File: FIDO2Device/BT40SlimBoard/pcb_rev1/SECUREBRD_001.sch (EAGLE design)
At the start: 32 parts, among them CN1 2137160001, CN2 IF_4PIN, CN4 IF_3PIN_SOL, SW3 SKTADAE010, SW4 SKRPACE010, SW5 SKRPACE010, U1 BT40, U2 XC6206P332MR-G

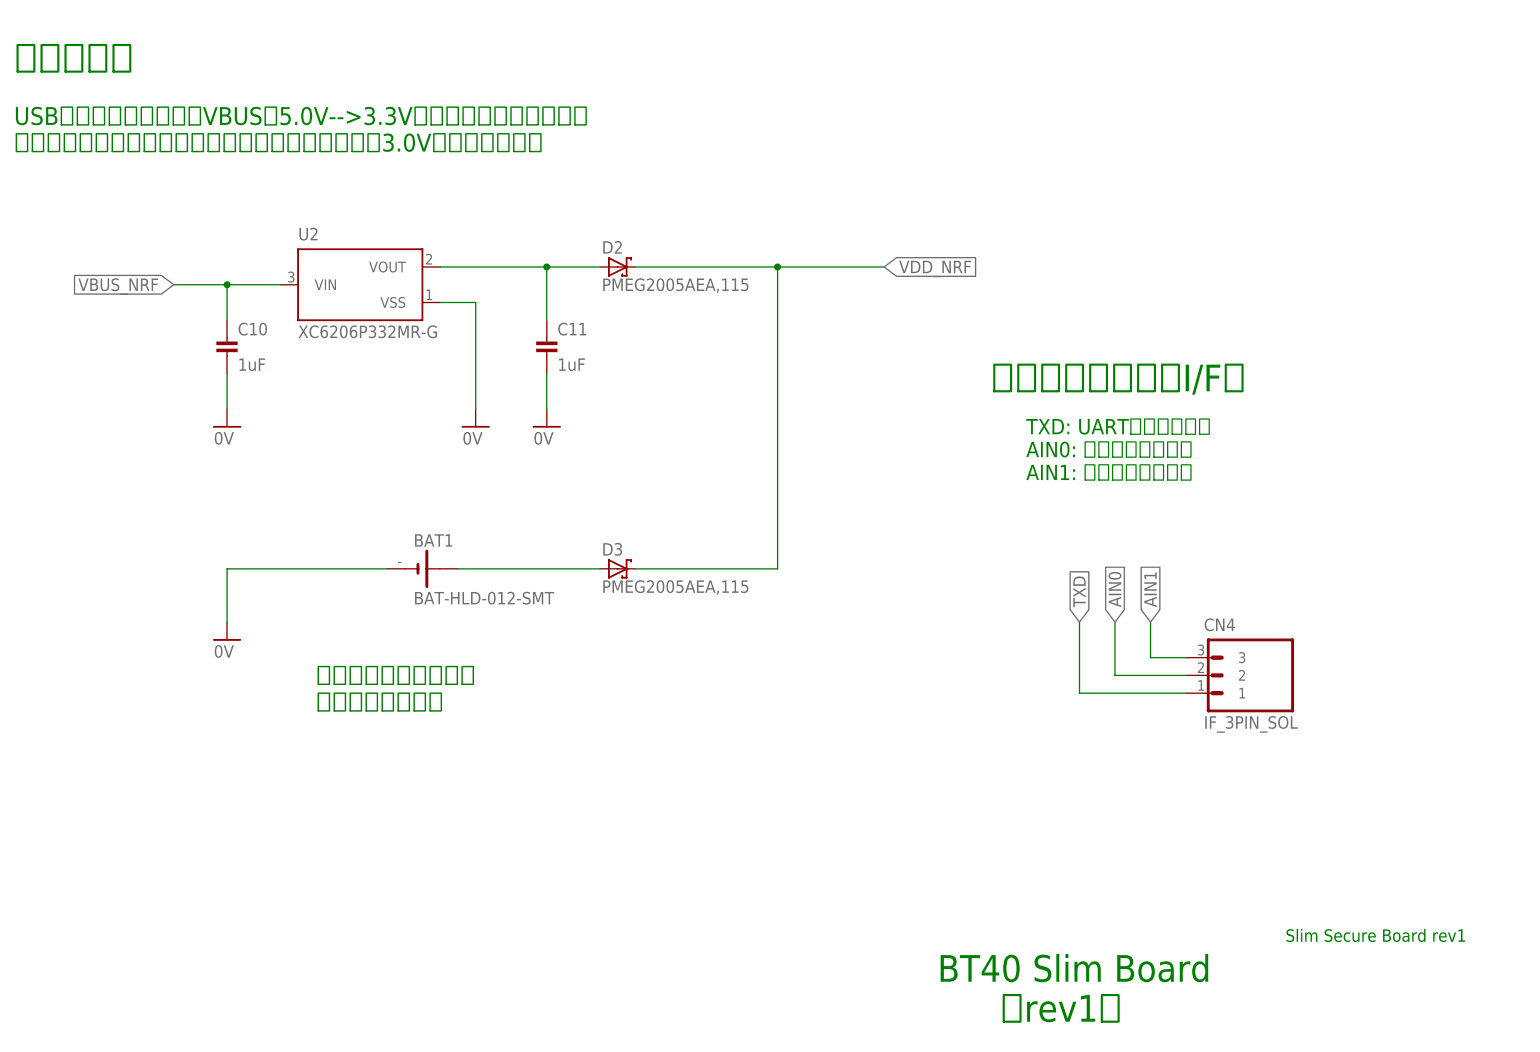
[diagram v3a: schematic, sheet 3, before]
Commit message: 回路図を更新
・降圧器を「ADP122ACPZ-3.3-R7」に差し替え
（小型化＆部品入手性を考慮した措置）
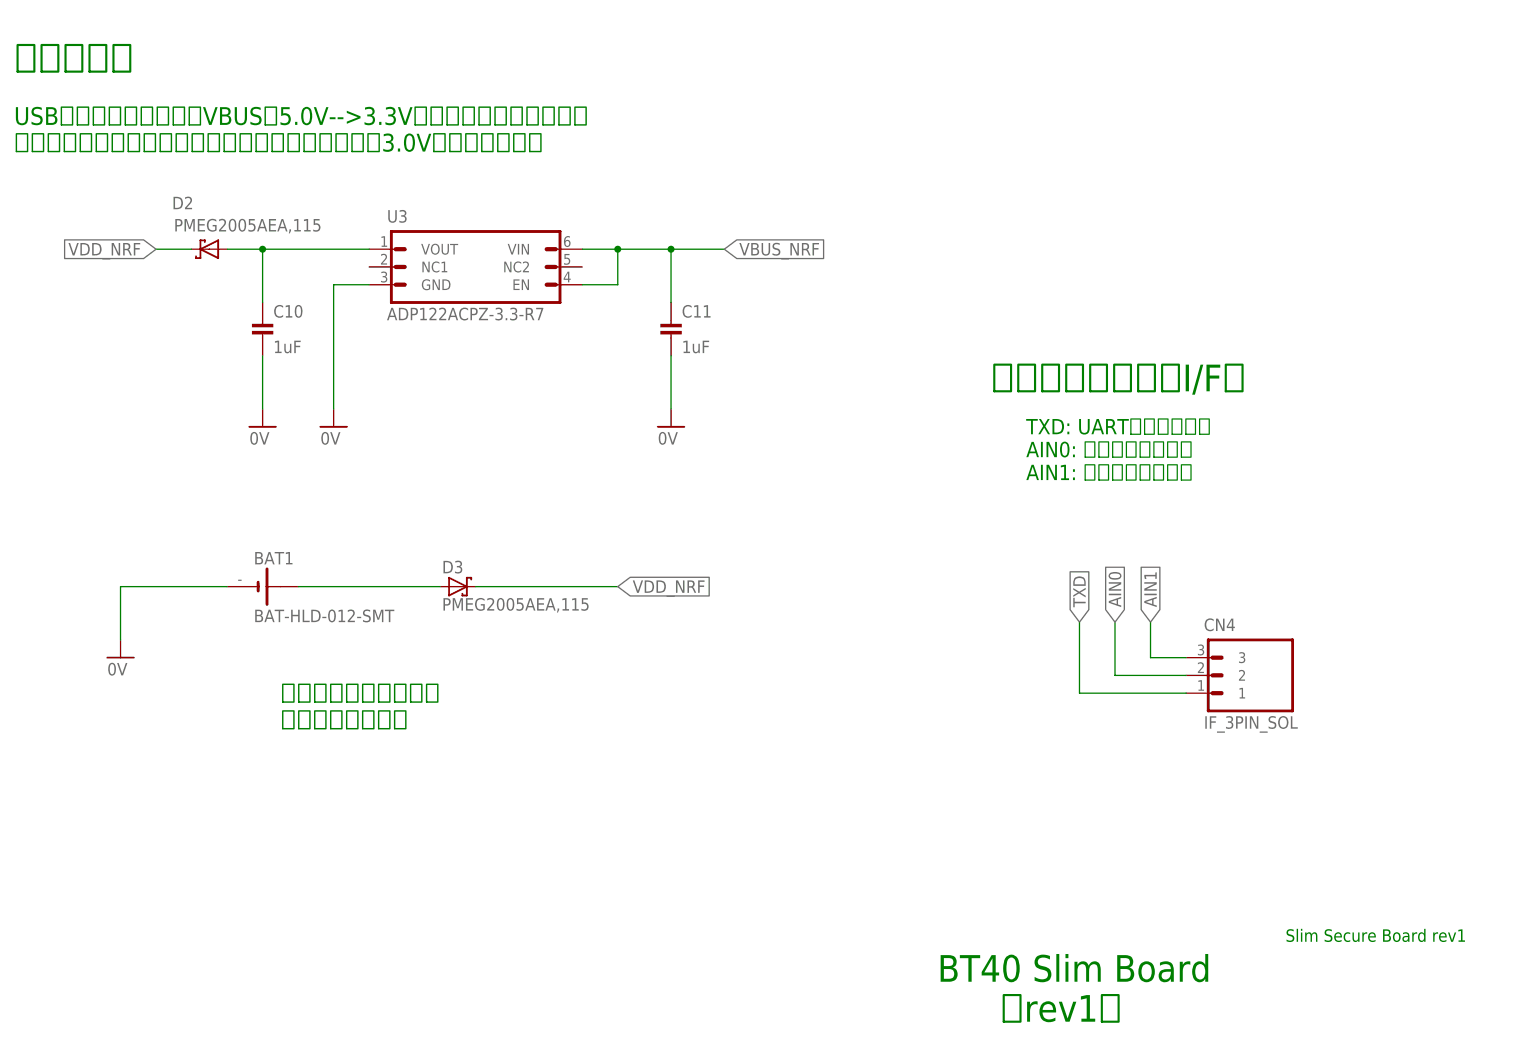
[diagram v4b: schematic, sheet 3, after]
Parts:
- removed U2: XC6206P332MR-G, Parts:XC6206P332MR-G
- added U3: ADP122ACPZ-3.3-R7, ICs:ADP122ACPZ-3.3-R7
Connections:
- removed net N$4: C11.1, D2.A, U2.VOUT
- new net N$3: C10.1, D2.A, U3.VOUT
- net 0V: now also U3.GND; no longer U2.VSS
- net VBUS_NRF: now also C11.1, U3.EN, U3.VIN; no longer C10.1, U2.VIN
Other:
- moved on the sheet: BAT1, C10, C11, D2, D3
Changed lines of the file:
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@@
 <setting verticaltext="up"/>
 </settings>
-<grid distance="0.1" unitdist="inch" unit="inch" style="lines" multiple="1" display="no" altdistance="0.01" altunitdist="inch" altunit="inch"/>
+<grid distance="0.1" unitdist="inch" unit="inch" style="lines" multiple="1" display="yes" altdistance="0.01" altunitdist="inch" altunit="inch"/>
 <layers>
 <layer number="1" name="Top" color="4" fill="1" visible="no" active="no"/>
@@
 <part name="LD2" library="Parts" deviceset="APHD1608" device="LSURCK"/>
 <part name="LD4" library="Parts" deviceset="APTD1608" device="LVBC/D"/>
-<part name="U2" library="Parts" deviceset="XC6206" device="P332MR-G"/>
 <part name="C10" library="Parts" deviceset="CAP" device="_0603" value="1uF"/>
 <part name="C11" library="Parts" deviceset="CAP" device="_0603" value="1uF"/>
@@
 <part name="CN1" library="Connectors" deviceset="2137160001" device=""/>
 <part name="R2" library="Parts" deviceset="RESISTOR" device="_0402" value="5.1k"/>
+<part name="U3" library="ICs" deviceset="ADP122" device="ACPZ-3.3-R7"/>
 </parts>
 <sheets>
@@
 <text x="35.56" y="139.7" size="2.54" layer="91" align="top-left">USBポートに装着時は、VBUSの5.0V--&gt;3.3Vに降圧して供給します。
 乾電池ホルダーにボタン乾電池を装着した場合は、3.0Vを供給します。</text>
-<text x="78.74" y="53.34" size="2.54" layer="91">ボタン乾電池ケースは
+<text x="73.66" y="50.8" size="2.54" layer="91">ボタン乾電池ケースは
 基板の表面に実装</text>
 <text x="175.26" y="99.06" size="3.81" layer="91">ユーティリティーI/F部</text>
@@
 <instances>
 <instance part="FRAME3" gate="G$1" x="0" y="0"/>
-<instance part="U2" gate="G$1" x="73.66" y="116.84"/>
-<instance part="C10" gate="G$1" x="66.04" y="109.22"/>
-<instance part="C11" gate="G$1" x="111.76" y="109.22"/>
-<instance part="GND16" gate="1" x="101.6" y="93.98"/>
-<instance part="GND17" gate="1" x="66.04" y="93.98"/>
-<instance part="GND18" gate="1" x="111.76" y="93.98"/>
-<instance part="D2" gate="G$1" x="121.92" y="116.84"/>
-<instance part="D3" gate="G$1" x="121.92" y="73.66"/>
-<instance part="BAT1" gate="G$1" x="93.98" y="73.66"/>
-<instance part="GND19" gate="1" x="66.04" y="63.5"/>
+<instance part="C10" gate="G$1" x="71.12" y="111.76"/>
+<instance part="C11" gate="G$1" x="129.54" y="111.76"/>
+<instance part="GND16" gate="1" x="71.12" y="93.98"/>
+<instance part="GND17" gate="1" x="81.28" y="93.98"/>
+<instance part="GND18" gate="1" x="129.54" y="93.98"/>
+<instance part="D2" gate="G$1" x="63.5" y="119.38" smashed="yes" rot="R180">
+<attribute name="NAME" x="58.166" y="125.095" size="1.778" layer="95"/>
+<attribute name="VALUE" x="58.42" y="121.92" size="1.778" layer="96"/>
+</instance>
+<instance part="D3" gate="G$1" x="99.06" y="71.12"/>
+<instance part="BAT1" gate="G$1" x="71.12" y="71.12"/>
+<instance part="GND19" gate="1" x="50.8" y="60.96"/>
 <instance part="CN4" gate="G$1" x="203.2" y="60.96"/>
+<instance part="U3" gate="G$1" x="86.36" y="116.84"/>
 </instances>
 <busses>
@@
 <net name="0V" class="0">
 <segment>
-<pinref part="C10" gate="G$1" pin="2"/>
-<pinref part="GND17" gate="1" pin="0V"/>
-<wire x1="66.04" y1="101.6" x2="66.04" y2="96.52" width="0.1524" layer="91"/>
-</segment>
-<segment>
-<pinref part="U2" gate="G$1" pin="VSS"/>
-<pinref part="GND16" gate="1" pin="0V"/>
-<wire x1="96.52" y1="111.76" x2="101.6" y2="111.76" width="0.1524" layer="91"/>
-<wire x1="101.6" y1="111.76" x2="101.6" y2="96.52" width="0.1524" layer="91"/>
+<pinref part="BAT1" gate="G$1" pin="-"/>
+<pinref part="GND19" gate="1" pin="0V"/>
+<wire x1="66.04" y1="71.12" x2="50.8" y2="71.12" width="0.1524" layer="91"/>
+<wire x1="50.8" y1="71.12" x2="50.8" y2="63.5" width="0.1524" layer="91"/>
 </segment>
 <segment>
 <pinref part="C11" gate="G$1" pin="2"/>
 <pinref part="GND18" gate="1" pin="0V"/>
-<wire x1="111.76" y1="101.6" x2="111.76" y2="96.52" width="0.1524" layer="91"/>
-</segment>
-<segment>
-<pinref part="BAT1" gate="G$1" pin="-"/>
-<pinref part="GND19" gate="1" pin="0V"/>
-<wire x1="88.9" y1="73.66" x2="66.04" y2="73.66" width="0.1524" layer="91"/>
-<wire x1="66.04" y1="73.66" x2="66.04" y2="66.04" width="0.1524" layer="91"/>
-</segment>
-</net>
-<net name="N$4" class="0">
-<segment>
-<pinref part="U2" gate="G$1" pin="VOUT"/>
-<wire x1="96.52" y1="116.84" x2="111.76" y2="116.84" width="0.1524" layer="91"/>
+<wire x1="129.54" y1="104.14" x2="129.54" y2="96.52" width="0.1524" layer="91"/>
+</segment>
+<segment>
+<pinref part="GND16" gate="1" pin="0V"/>
+<pinref part="C10" gate="G$1" pin="2"/>
+<wire x1="71.12" y1="96.52" x2="71.12" y2="104.14" width="0.1524" layer="91"/>
+</segment>
+<segment>
+<pinref part="GND17" gate="1" pin="0V"/>
+<wire x1="81.28" y1="96.52" x2="81.28" y2="114.3" width="0.1524" layer="91"/>
+<pinref part="U3" gate="G$1" pin="GND"/>
+<wire x1="81.28" y1="114.3" x2="86.36" y2="114.3" width="0.1524" layer="91"/>
+</segment>
+</net>
+<net name="VBUS_NRF" class="0">
+<segment>
+<wire x1="116.84" y1="119.38" x2="121.92" y2="119.38" width="0.1524" layer="91"/>
+<label x="137.16" y="119.38" size="1.778" layer="95" xref="yes"/>
+<pinref part="U3" gate="G$1" pin="VIN"/>
+<pinref part="U3" gate="G$1" pin="EN"/>
+<wire x1="121.92" y1="119.38" x2="129.54" y2="119.38" width="0.1524" layer="91"/>
+<wire x1="129.54" y1="119.38" x2="137.16" y2="119.38" width="0.1524" layer="91"/>
+<wire x1="116.84" y1="114.3" x2="121.92" y2="114.3" width="0.1524" layer="91"/>
+<wire x1="121.92" y1="114.3" x2="121.92" y2="119.38" width="0.1524" layer="91"/>
+<junction x="121.92" y="119.38"/>
 <pinref part="C11" gate="G$1" pin="1"/>
-<wire x1="111.76" y1="116.84" x2="119.38" y2="116.84" width="0.1524" layer="91"/>
-<wire x1="111.76" y1="116.84" x2="111.76" y2="109.22" width="0.1524" layer="91"/>
-<junction x="111.76" y="116.84"/>
-<pinref part="D2" gate="G$1" pin="A"/>
-</segment>
-</net>
-<net name="VBUS_NRF" class="0">
-<segment>
-<pinref part="U2" gate="G$1" pin="VIN"/>
-<pinref part="C10" gate="G$1" pin="1"/>
-<wire x1="73.66" y1="114.3" x2="66.04" y2="114.3" width="0.1524" layer="91"/>
-<wire x1="66.04" y1="114.3" x2="66.04" y2="109.22" width="0.1524" layer="91"/>
-<wire x1="66.04" y1="114.3" x2="58.42" y2="114.3" width="0.1524" layer="91"/>
-<junction x="66.04" y="114.3"/>
-<label x="58.42" y="114.3" size="1.778" layer="95" rot="R180" xref="yes"/>
+<wire x1="129.54" y1="119.38" x2="129.54" y2="111.76" width="0.1524" layer="91"/>
+<junction x="129.54" y="119.38"/>
 </segment>
 </net>
 <net name="VDD_NRF" class="0">
 <segment>
-<wire x1="124.46" y1="116.84" x2="144.78" y2="116.84" width="0.1524" layer="91"/>
-<label x="160.02" y="116.84" size="1.778" layer="95" xref="yes"/>
+<label x="121.92" y="71.12" size="1.778" layer="95" xref="yes"/>
+<pinref part="D3" gate="G$1" pin="C"/>
+<wire x1="101.6" y1="71.12" x2="121.92" y2="71.12" width="0.1524" layer="91"/>
+</segment>
+<segment>
 <pinref part="D2" gate="G$1" pin="C"/>
-<pinref part="D3" gate="G$1" pin="C"/>
-<wire x1="144.78" y1="116.84" x2="160.02" y2="116.84" width="0.1524" layer="91"/>
-<wire x1="124.46" y1="73.66" x2="144.78" y2="73.66" width="0.1524" layer="91"/>
-<wire x1="144.78" y1="73.66" x2="144.78" y2="116.84" width="0.1524" layer="91"/>
-<junction x="144.78" y="116.84"/>
+<wire x1="60.96" y1="119.38" x2="55.88" y2="119.38" width="0.1524" layer="91"/>
+<label x="55.88" y="119.38" size="1.778" layer="95" rot="R180" xref="yes"/>
 </segment>
 </net>
@@
 <pinref part="BAT1" gate="G$1" pin="+"/>
 <pinref part="D3" gate="G$1" pin="A"/>
-<wire x1="99.06" y1="73.66" x2="119.38" y2="73.66" width="0.1524" layer="91"/>
+<wire x1="76.2" y1="71.12" x2="96.52" y2="71.12" width="0.1524" layer="91"/>
 </segment>
 </net>
@@
 </segment>
 </net>
+<net name="N$3" class="0">
+<segment>
+<pinref part="U3" gate="G$1" pin="VOUT"/>
+<pinref part="D2" gate="G$1" pin="A"/>
+<wire x1="86.36" y1="119.38" x2="71.12" y2="119.38" width="0.1524" layer="91"/>
+<pinref part="C10" gate="G$1" pin="1"/>
+<wire x1="71.12" y1="119.38" x2="66.04" y2="119.38" width="0.1524" layer="91"/>
+<wire x1="71.12" y1="119.38" x2="71.12" y2="111.76" width="0.1524" layer="91"/>
+<junction x="71.12" y="119.38"/>
+</segment>
+</net>
